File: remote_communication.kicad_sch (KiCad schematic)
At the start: 1 part

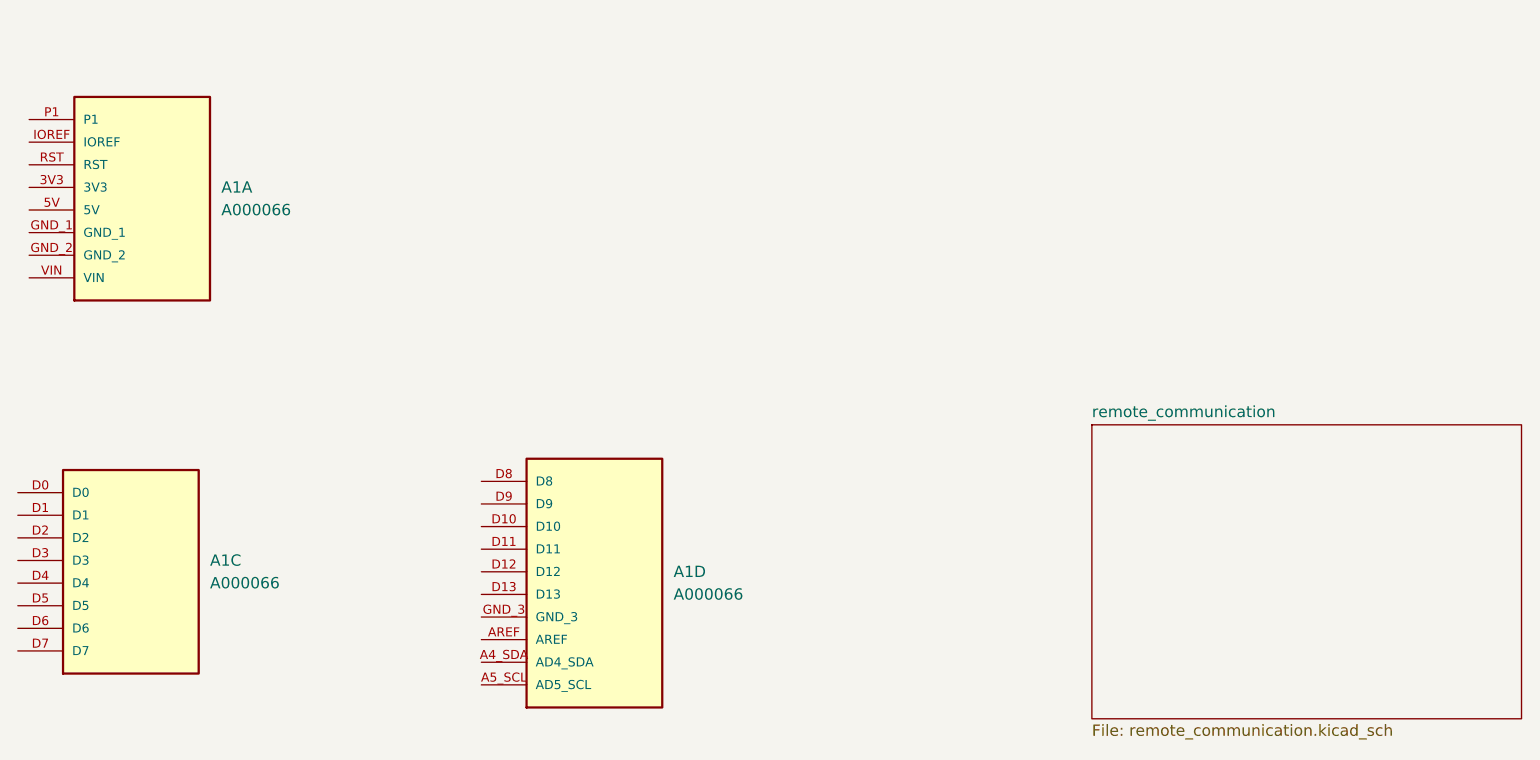
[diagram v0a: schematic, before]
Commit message: Move remote communication system to hierarchal page
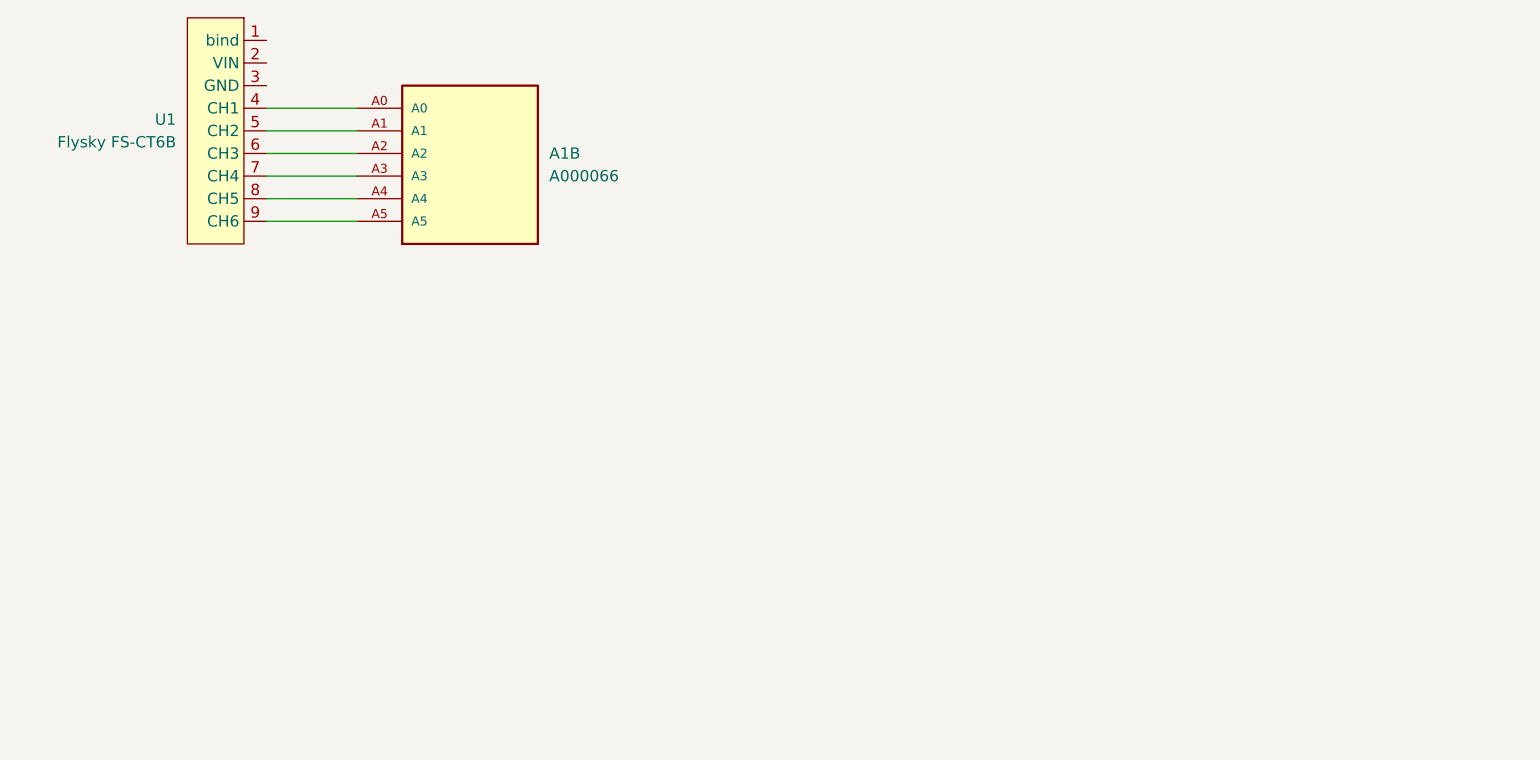
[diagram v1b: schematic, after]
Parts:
- removed A1: A000066, A000066:ARDUINO_A000066, symbol A000066:A000066
- added A1: A000066, A000066:ARDUINO_A000066, symbol A000066:A000066
- added U1: Flysky FS-CT6B, symbol battlebot_library:FS-CT6B_Receiver
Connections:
- new net: A1.A0, U1.4 (CH1)
- new net: A1.A1, U1.5 (CH2)
- new net: A1.A2, U1.6 (CH3)
- new net: A1.A3, U1.7 (CH4)
- new net: A1.A4, U1.8 (CH5)
- new net: A1.A5, U1.9 (CH6)
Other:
- removed sheet remote_communication

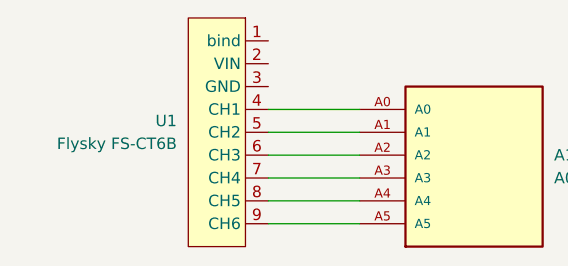
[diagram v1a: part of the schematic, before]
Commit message: Fix remote_communications schematic having wrong Arduino unit
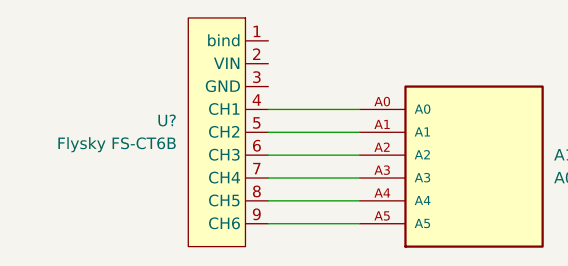
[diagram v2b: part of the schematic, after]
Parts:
- renumbered U1 to U?
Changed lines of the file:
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@@
 		(on_board yes)
 		(dnp no)
-		(property "Reference" "U1"
+		(property "Reference" "U?"
 			(at 35.56 31.7499 0)
 			(effects
@@
 		)
 		(instances
+			(project "remote_communication"
+				(path "/14fcab28-600e-4979-89c6-942868a89dab"
+					(reference "U?")
+					(unit 1)
+				)
+			)
 			(project "battlebot-system"
 				(path "/a350ff7a-a547-44b8-aa5d-3d9eed7f09e0/f5681333-f861-4eb9-b596-a5fc6c6c8feb"
@@
 		)
 		(instances
+			(project "remote_communication"
+				(path "/14fcab28-600e-4979-89c6-942868a89dab"
+					(reference "A1")
+					(unit 2)
+				)
+			)
 			(project "battlebot-system"
 				(path "/a350ff7a-a547-44b8-aa5d-3d9eed7f09e0/f5681333-f861-4eb9-b596-a5fc6c6c8feb"
@@
 		)
 	)
+	(sheet_instances
+		(path "/"
+			(page "1")
+		)
+	)
+	(embedded_fonts no)
 )

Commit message: Add A000066 symbol library locally to project
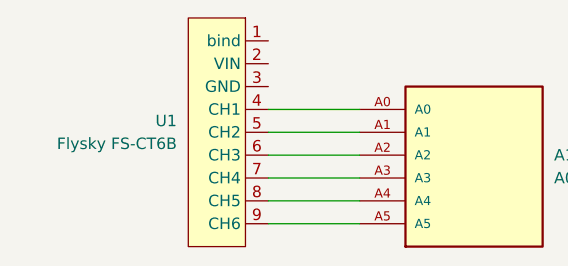
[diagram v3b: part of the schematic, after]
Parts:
- gave numbers to parts that had none: 1
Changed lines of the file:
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@@
-	(wire
-		(pts
-			(xy 45.72 43.18) (xy 55.88 43.18)
-		)
-		(stroke
-			(width 0)
-			(type default)
-		)
-	)
 	(wire
 		(pts
@@
 		(pts
 			(xy 45.72 33.02) (xy 55.88 33.02)
+		)
+		(stroke
+			(width 0)
+			(type default)
+		)
+	)
+	(wire
+		(pts
+			(xy 45.72 43.18) (xy 55.88 43.18)
 		)
 		(stroke
@@
 		(on_board yes)
 		(dnp no)
-		(property "Reference" "U?"
+		(property "Reference" "U1"
 			(at 35.56 31.7499 0)
 			(effects
